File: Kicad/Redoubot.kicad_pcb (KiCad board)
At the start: 4 copper layers, 90 x 72.5 mm, 99 parts, among them J1 HM_10_BLE_Module, J10 VL53L0CXV0DH - TOF, J11 DFPlayer_Left, J12 Speaker, J13 DFPlayer_Right, J14 USB_C_Receptacle_USB2.0_16P, J15 Conn_ST_STDC14, J2 Connecteur batterie, J3 APDS9960, J4 Neopixel, J5 Motor_Left, J6 Motor_Right, J7 MPU-6050, J8 Servo_Left, J9 Servo_Right, Q1 DMP1045UQ-7, U1 STM32G431RBTx, U2 LD39050PU33R, U3 BQ25896RTWR, U4 BQ27220YZFR, U5 DRV8833PWP, U7 DMN313DLT-7, U8 MMDT2907A-7-F, Y1 8MHz

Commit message: chore: silkscreen fix
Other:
- board text added: "E-MENPIOT G-LOISELET G-VIDON J-MANSARD L-FIACK"
- board text removed: "E-MENPIOT G-LOISELET G-VIDON J-MANSARD L-FIACK {dblquote}---->"
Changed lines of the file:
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@@
 		(tags "capacitor")
 		(property "Reference" "C42"
-			(at 0 -1.16 90)
+			(at -0.05 -1.65 90)
 			(layer "F.SilkS")
 			(effects
@@
 		(tags "capacitor")
 		(property "Reference" "C40"
-			(at 0 -1.16 90)
+			(at -0.450001 -1.625 90)
 			(layer "F.SilkS")
 			(effects
@@
 		)
 	)
-	(gr_text "E-MENPIOT\nG-LOISELET\nG-VIDON\nJ-MANSARD\n\nL-FIACK\n {dblquote}---->"
+	(gr_text "E-MENPIOT\nG-LOISELET\nG-VIDON\nJ-MANSARD\n\nL-FIACK"
 		(at 114 125.6 0)
 		(layer "F.SilkS")
@@
 	)
 	(segment
-		(start 136.942436 101.85)
-		(end 139.780761 101.85)
+		(start 138.75 101.25)
+		(end 144.546447 101.25)
 		(width 0.3)
 		(layer "B.Cu")
@@
 	)
 	(segment
-		(start 144.546447 101.25)
-		(end 153.196447 92.6)
+		(start 136.942436 101.85)
+		(end 138.15 101.85)
 		(width 0.3)
 		(layer "B.Cu")
@@
 	)
 	(segment
-		(start 140.380761 101.25)
-		(end 144.546447 101.25)
+		(start 144.546447 101.25)
+		(end 153.196447 92.6)
 		(width 0.3)
 		(layer "B.Cu")
@@
 	)
 	(segment
-		(start 139.780761 101.85)
-		(end 140.380761 101.25)
+		(start 138.15 101.85)
+		(end 138.75 101.25)
 		(width 0.3)
 		(layer "B.Cu")
@@
 	)
 	(segment
-		(start 152.55 85.2)
+		(start 153 84.8)
 		(end 152.95 84.8)
 		(width 0.3)
@@
 	(segment
 		(start 152.95 84.8)
-		(end 153 84.8)
+		(end 152.55 85.2)
 		(width 0.3)
 		(layer "B.Cu")
@@
 	)
 	(segment
-		(start 147.2 85.2)
-		(end 152.55 85.2)
+		(start 152.55 85.2)
+		(end 147.2 85.2)
 		(width 0.3)
 		(layer "B.Cu")
@@
 	)
 	(segment
+		(start 127.675 69.3)
+		(end 128.035 69.66)
+		(width 0.2)
+		(layer "F.Cu")
+		(net "/Power_management/BAT_CHG")
+	)
+	(segment
+		(start 127.189999 69.3)
+		(end 127.675 69.3)
+		(width 0.2)
+		(layer "F.Cu")
+		(net "/Power_management/BAT_CHG")
+	)
+	(segment
 		(start 126.8875 69.3)
 		(end 126.630754 69.043254)
@@
 	)
 	(segment
-		(start 127.189999 69.3)
-		(end 127.65 69.3)
-		(width 0.2)
-		(layer "F.Cu")
-		(net "/Power_management/BAT_CHG")
-	)
-	(segment
-		(start 128.035 69.685)
-		(end 128.035 71.865001)
+		(start 126.875 69.614999)
+		(end 127.189999 69.3)
 		(width 0.2)
 		(layer "F.Cu")
@@
 	)
 	(segment
-		(start 127.65 69.3)
-		(end 128.035 69.685)
-		(width 0.2)
-		(layer "F.Cu")
-		(net "/Power_management/BAT_CHG")
-	)
-	(segment
 		(start 138.475 83.425)
 		(end 138.475 84.320001)
@@
 	)
 	(segment
-		(start 126.875 69.614999)
-		(end 127.189999 69.3)
+		(start 128.035 69.66)
+		(end 128.035 71.865001)
 		(width 0.2)
 		(layer "F.Cu")
@@
 	)
 	(segment
+		(start 128.535 69.665)
+		(end 128.535 71.865)
+		(width 0.2)
+		(layer "F.Cu")
+		(net "/Power_management/BAT")
+	)
+	(segment
 		(start 124.113491 69.213491)
 		(end 125.154999 70.254999)
@@
 	)
 	(segment
-		(start 128.8 69.3)
-		(end 128.535 69.565)
+		(start 129.485001 69.3)
+		(end 128.9 69.3)
+		(width 0.2)
+		(layer "F.Cu")
+		(net "/Power_management/BAT")
+	)
+	(segment
+		(start 128.9 69.3)
+		(end 128.535 69.665)
 		(width 0.2)
 		(layer "F.Cu")
@@
 	)
 	(segment
-		(start 129.485001 69.3)
-		(end 128.8 69.3)
-		(width 0.2)
-		(layer "F.Cu")
-		(net "/Power_management/BAT")
-	)
-	(segment
 		(start 125.7675 71.165)
 		(end 125.7675 70.854009)
@@
 		(layer "F.Cu")
 		(net "/Power_management/BAT")
-	)
-	(segment
-		(start 128.535 69.565)
-		(end 128.535 71.865)
-		(width 0.2)
-		(layer "F.Cu")
-		(net "/Power_management/BAT")

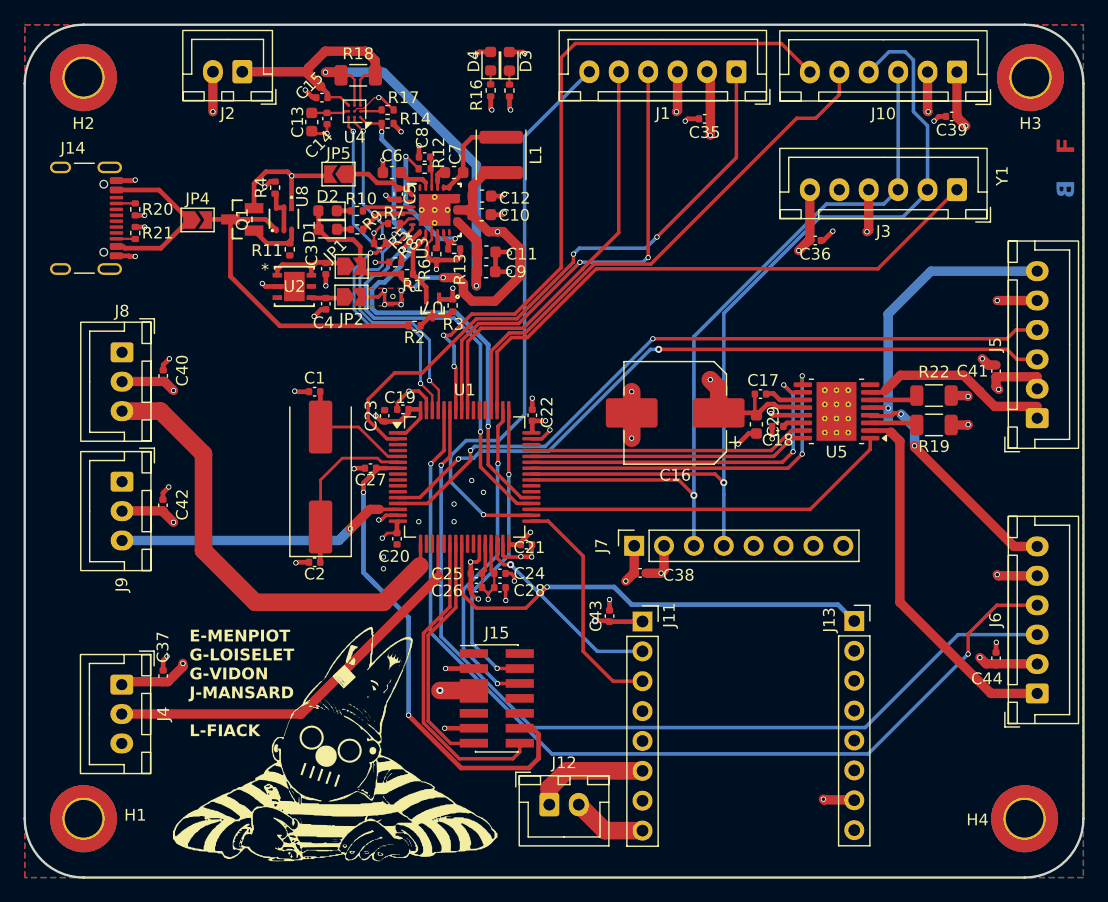
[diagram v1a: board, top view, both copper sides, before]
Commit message: Chore: fixed warnings and errors. Removed built in vias to replace with properly sized ones
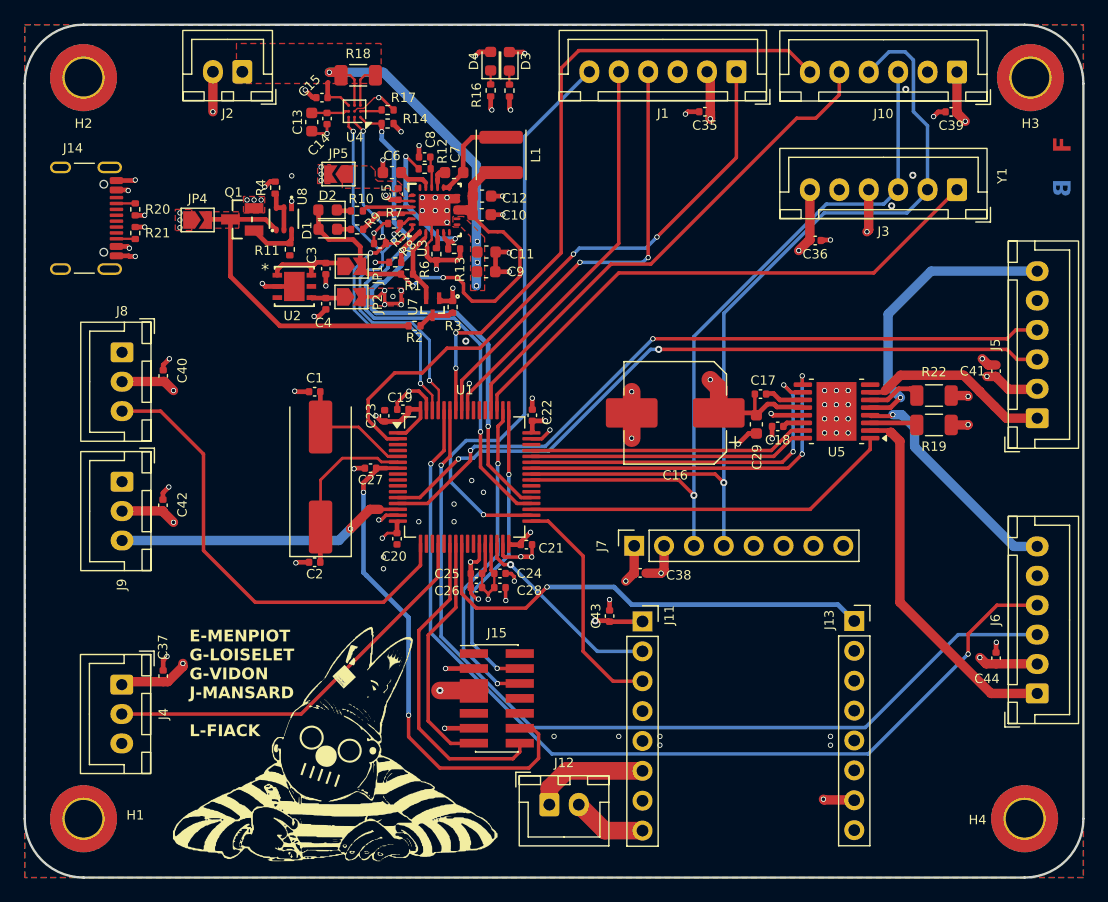
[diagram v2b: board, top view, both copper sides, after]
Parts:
- moved C35 0.60 mm to (157.8, 72.4)
- moved C39 0.39 mm to (178.8, 72.4)
- moved R3 0.14 mm to (136.4, 89.0)
- moved D2 0.07 mm to (125.8, 80.8)
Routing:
- net /Power_management/BAT: track 23.4 -> 7.46 mm
- net GND: track 128.2 -> 113.7 mm, vias 68 -> 94
- net Net-(JP4-A): track 14.7 -> 2.18 mm, vias 0 -> 5
- net +5V: track 202.0 -> 190.7 mm, vias 9 -> 16
- net /Power_management/BAT_CHG: track 38.2 -> 31.5 mm, vias 2 -> 4
- net Net-(JP5-A): track 6.43 -> 0.00 mm
- net /XSHUT_TOF: track 59.7 -> 56.6 mm
- net /INT_ADA: track 49.8 -> 47.6 mm
- net /RXD_HM10: track 36.2 -> 34.1 mm
- net /TXD_HM10: track 40.5 -> 38.5 mm
- net /GPIO_TOF: track 45.6 -> 43.9 mm
- net /STM32/STLINK_TX: track 26.6 -> 27.4 mm
- net VCC: track 39.3 -> 38.9 mm, vias 3 -> 2
- net /Motor_Driver/MR-: track 20.0 -> 19.8 mm, vias 2 -> 1
- added copper zone on F.Cu, net +5V
- added copper zone on F.Cu, net /Power_management/BAT
- added copper zone on F.Cu, net /Power_management/BAT_CHG
- added copper zone on F.Cu, net Net-(JP4-A)
- added copper zone on In2.Cu, net Net-(JP4-A)
- added copper zone on F.Cu, net Net-(JP5-A)
- added copper zone on F.Cu, net VBUS

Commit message: chore: added the positions.csv file for JLCPCB
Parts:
- Y1: footprint Crystal:Crystal_SMD_HC49-SD -> Crystal:Crystal_SMD_5032-2Pin_5.0x3.2mm
- moved C2 5.85 mm to (124.7, 104.8)
- moved Y1 2.42 mm to (125.1, 101.0)
- moved C1 1.15 mm to (124.7, 97.3)
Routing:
- net Net-(U1-PF1): track 14.5 -> 8.87 mm
- net Net-(U1-PF0): track 10.6 -> 9.47 mm
- net GND: track 113.7 -> 112.7 mm
